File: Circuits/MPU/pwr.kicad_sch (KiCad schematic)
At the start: 97 parts, among them Q7 MMBT2222A, Q8 MMBT2222A, T1 HPH1-1400L, U1 ProASIC, U16 DG403, U17 REF43GS, U18 ADA4805-2ARMZ, U19 ADA4805-2ARMZ

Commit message: LVDS I/F for HV
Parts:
- U1: desc FPGA -> FPGA; manf# (none) -> A3PE3000-FGG484
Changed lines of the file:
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@@
 			)
 		)
-		(property "Datasheet" "	https://www.microsemi.com/document-portal/doc_download/130701-ds0098-proasic3e-flash-family-fpgas-datasheet"
+		(property "Datasheet" "https://www.microsemi.com/document-portal/doc_download/130701-ds0098-proasic3e-flash-family-fpgas-datasheet"
 			(at 30.48 64.77 0)
 			(effects
@@
 			)
 		)
-		(property "desc" "	FPGA"
+		(property "desc" "FPGA"
 			(at 30.48 62.23 0)
 			(effects
@@
 			)
 		)
+		(property "manf#" "A3PE3000-FGG484"
+			(at 30.48 67.31 0)
+			(effects
+				(font
+					(size 1.27 1.27)
+				)
+				(justify left)
+				(hide yes)
+			)
+		)
 		(pin "R22"
 		)
@@
 		(pin "A4"
 		)
+		(pin "P19"
+		)
+		(pin "P21"
+		)
+		(pin "R19"
+		)
+		(pin "R21"
+		)
+		(pin "T20"
+		)
+		(pin "T21"
+		)
+		(pin "U20"
+		)
+		(pin "U21"
+		)
+		(pin "V21"
+		)
+		(pin "W21"
+		)
 		(instances

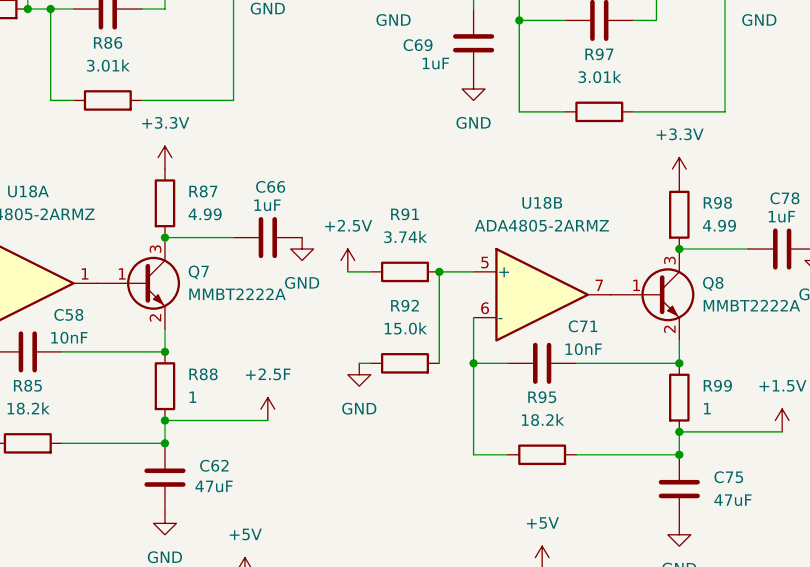
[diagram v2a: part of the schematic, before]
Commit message: Fix errors found by Norm Dobson
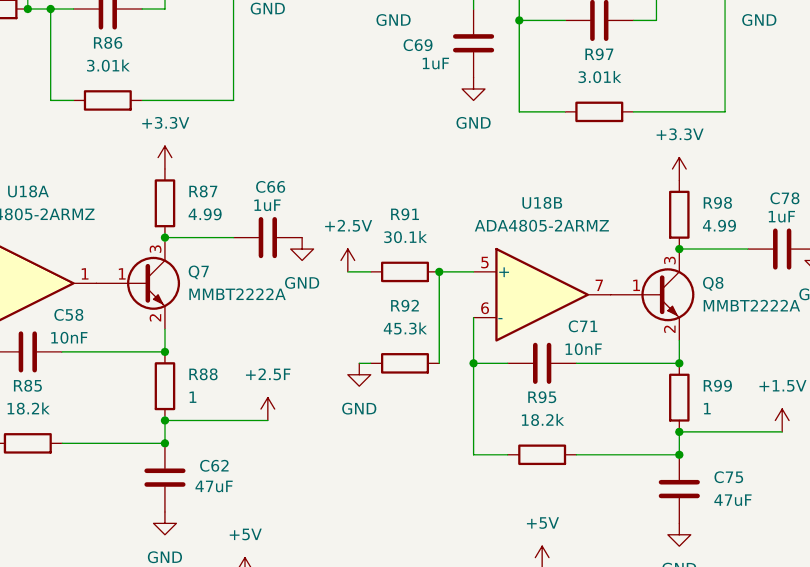
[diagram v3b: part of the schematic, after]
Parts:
- R91: value 3.74k -> 30.1k
- R92: value 15.0k -> 45.3k
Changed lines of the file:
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@@
 			)
 		)
-		(property "Value" "3.74k"
+		(property "Value" "30.1k"
 			(at 218.44 102.87 90)
 			(effects
@@
 			)
 		)
-		(property "Value" "15.0k"
+		(property "Value" "45.3k"
 			(at 218.44 113.03 90)
 			(effects
